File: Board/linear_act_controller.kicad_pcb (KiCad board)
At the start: 4 copper layers, 90 x 40 mm, 71 parts, among them J1 SSV, J2 ACTUATOR, J3 PROG, U1 LMR51635XDDCR, U2 MP2459, U3 MP6612, U4 STM32F030K6Tx

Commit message: WIP on routing
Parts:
- removed D6: PWR, LED_SMD:LED_0603_1608Metric_Pad1.05x0.95mm_HandSolder
- removed D7: DBG, LED_SMD:LED_0603_1608Metric
- added H1: MountingHole_Pad, MountingHole:MountingHole_3.5mm_Pad_Via, F.Cu at (59.0, 84.0)
- added H2: MountingHole_Pad, MountingHole:MountingHole_3.5mm_Pad_Via, F.Cu at (59.0, 116.0)
- added H3: MountingHole_Pad, MountingHole:MountingHole_3.5mm_Pad_Via, F.Cu at (141.0, 116.0)
- added H4: MountingHole_Pad, MountingHole:MountingHole_3.5mm_Pad_Via, F.Cu at (141.0, 84.0)
- added J4: PWR_LED, Connector_JST:JST_XH_B2B-XH-A_1x02_P2.50mm_Vertical, F.Cu at (80.0, 85.2)
- added J5: STATUS_LED, Connector_JST:JST_XH_B2B-XH-A_1x02_P2.50mm_Vertical, F.Cu at (97.0, 85.3)
- added Q9: IRLML6344TRPBF, Package_TO_SOT_SMD:SOT-23_Handsoldering, F.Cu at (88.6, 85.4)
- added R36: 10k, Resistor_SMD:R_0603_1608Metric_Pad0.98x0.95mm_HandSolder, F.Cu at (88.6, 81.6)
- R16: value 47k -> 120
- R24: value 1k -> 120
- moved D1 209.6 mm to (65.8, 91.4), turned to 180 degrees
- moved R2 205.5 mm to (66.2, 89.6), turned to 180 degrees
- moved R1 205.3 mm to (66.2, 93.2)
- moved D5 181.6 mm to (105.6, 115.0), turned to -90 degrees
- moved C9 177.4 mm to (106.8, 108.7), turned to -90 degrees
- moved C11 176.8 mm to (101.6, 115.5), turned to -90 degrees
- moved R13 176.3 mm to (101.6, 111.8), turned to 90 degrees
- moved D4 175.0 mm to (109.8, 108.4), turned to -90 degrees
- moved U2 173.3 mm to (104.2, 109.7), turned to -90 degrees
- moved C10 169.9 mm to (103.2, 115.5), turned to -90 degrees
- moved R17 167.9 mm to (100.8, 106.4), turned to 180 degrees
- moved R15 166.9 mm to (104.2, 106.4), turned to 180 degrees
- moved R16 162.9 mm to (84.0, 84.4), turned to -90 degrees
- moved C13 161.6 mm to (110.0, 115.2), turned to -90 degrees
- moved L2 160.7 mm to (108.8, 111.8)
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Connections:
- L1 pad 1: Net-(U1-SW) -> +24V
- L1 pad 2: +24V -> Net-(U1-SW)
- R24 pad 1: Net-(U4-PA13) -> +3.3V
- TP2 pad 1: Net-(U4-PA13) -> STATUS_LED
- U4 pad 23: Net-(U4-PA13) -> STATUS_LED
- U4 pad 7: HB_VISEN -> POSITION_POT
- U4 pad 8: unconnected-(U4-PA2-Pad8) -> HB_VISEN
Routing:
- net +24V: track 0.00 -> 24.2 mm, vias 0 -> 2
- net +3.3V: track 0.00 -> 11.2 mm, vias 0 -> 2
- net Net-(D4-K): track 0.00 -> 5.21 mm
- net Net-(U1-EN): track 0.00 -> 3.92 mm
- net Net-(U2-FB): track 0.00 -> 3.70 mm
- net Net-(U1-FB): track 0.00 -> 3.69 mm
- net Net-(U1-CB): track 0.00 -> 2.44 mm
- net Net-(U1-SW): track 0.00 -> 2.12 mm
- net Net-(U2-EN): track 0.00 -> 1.71 mm
- added copper zone on F.Cu, net +24V
- added copper zone on B.Cu, net Net-(D3-K)
- added copper zone on F.Cu, net Net-(D3-K)
- added copper zone on F.Cu, net Net-(D5-K)
- added copper zone on B.Cu, net Net-(U1-SW)
- added copper zone on F.Cu, net Net-(U1-SW)
- added copper zone on B.Cu, net VIN
- added copper zone on F.Cu, net VIN

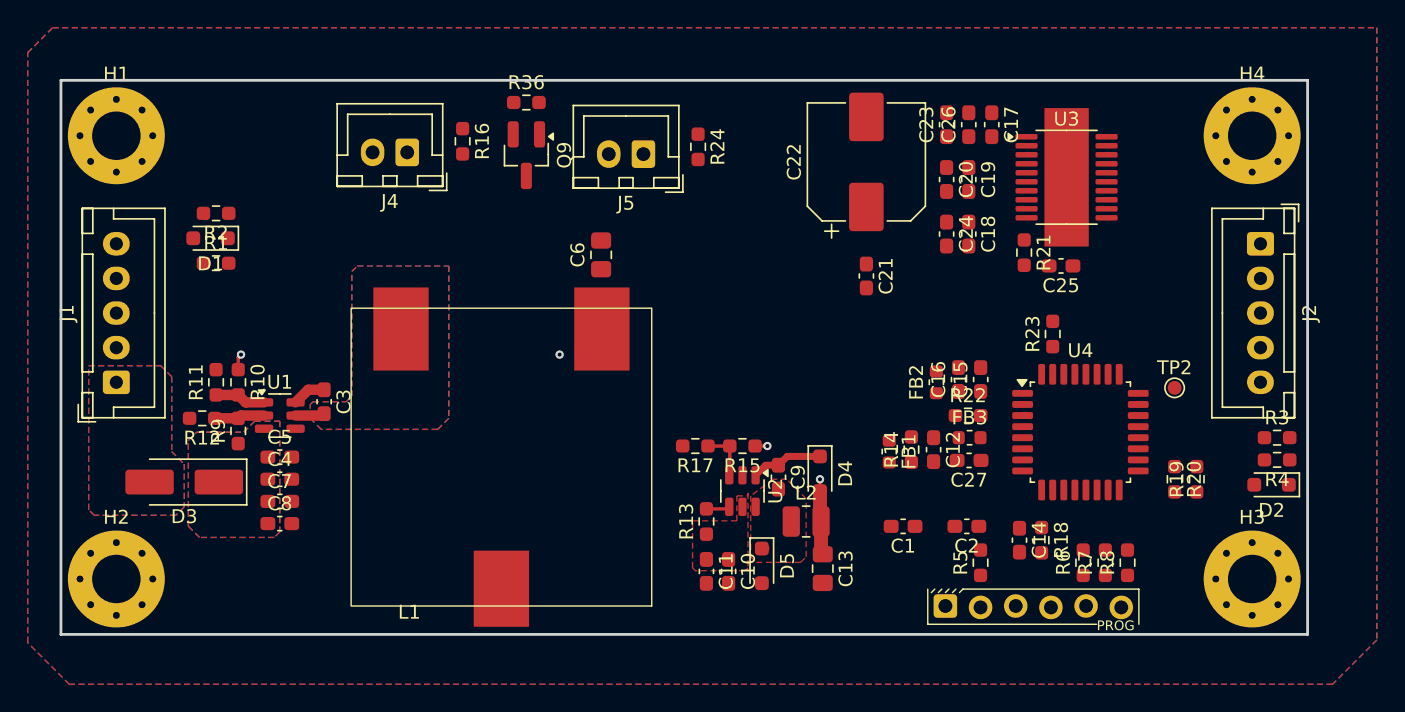
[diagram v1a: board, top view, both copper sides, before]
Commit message: Routing done, before adding polyfuse
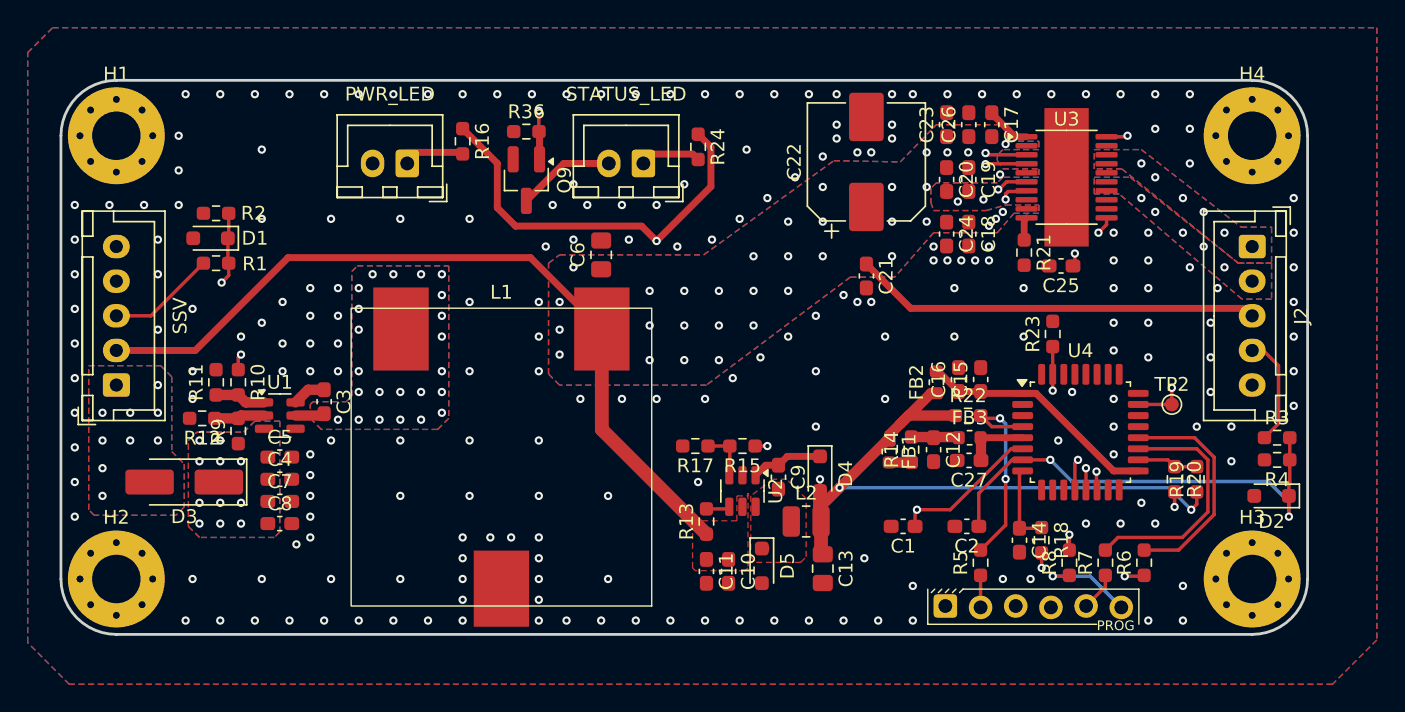
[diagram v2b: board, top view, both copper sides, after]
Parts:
- moved R6 4.40 mm to (133.2, 114.8)
- moved R8 4.20 mm to (127.8, 114.8)
- moved R36 2.10 mm to (88.6, 83.7)
- moved Q9 1.80 mm to (88.6, 87.2)
- moved TP2 1.22 mm to (135.2, 103.4)
- moved D2 0.80 mm to (142.4, 110.0)
- moved J4 0.80 mm to (80.0, 86.0)
- moved J5 0.67 mm to (97.0, 86.0)
- moved J2 0.63 mm to (141.0, 92.0)
- moved J1 0.20 mm to (59.0, 102.0)
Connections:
- L1 pad : (no net) -> GND
- U4 pad 12: HB_ENBL -> HB_DIR
- U4 pad 13: HB_DIR -> HB_ENBL
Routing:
- net +3.3V: track 11.2 -> 104.8 mm, vias 2 -> 5
- net +24V: track 24.2 -> 112.0 mm, vias 2 -> 36
- net CONTROL_POT: track 0.00 -> 75.7 mm, vias 0 -> 2
- net STATUS_LED: track 0.00 -> 70.5 mm, vias 0 -> 2
- net POSITION_POT: track 0.00 -> 33.8 mm, vias 0 -> 2
- net HB_ENBL: track 0.00 -> 31.6 mm, vias 0 -> 2
- net Net-(U3-VISEN): track 0.00 -> 31.0 mm, vias 0 -> 2
- net Net-(U3-nFAULT): track 0.00 -> 30.8 mm, vias 0 -> 2
- net HB_DIR: track 0.00 -> 30.7 mm, vias 0 -> 2
- net HB_nSLEEP: track 0.00 -> 20.0 mm, vias 0 -> 2
- net PROG_TX: track 0.00 -> 17.7 mm
- net /uC/3V3_STM: track 0.00 -> 17.6 mm
- net PROG_RX: track 0.00 -> 16.3 mm
- net PROG_NRST: track 0.00 -> 15.3 mm, vias 0 -> 2
- net PROG_BOOT0: track 0.00 -> 15.2 mm, vias 0 -> 2
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- added copper zone on B.Cu, net +24V
- added copper zone on B.Cu, net OUT1
- added copper zone on F.Cu, net OUT1
- added copper zone on B.Cu, net OUT2
- added copper zone on F.Cu, net OUT2
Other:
- outline, holes or cut-outs redrawn

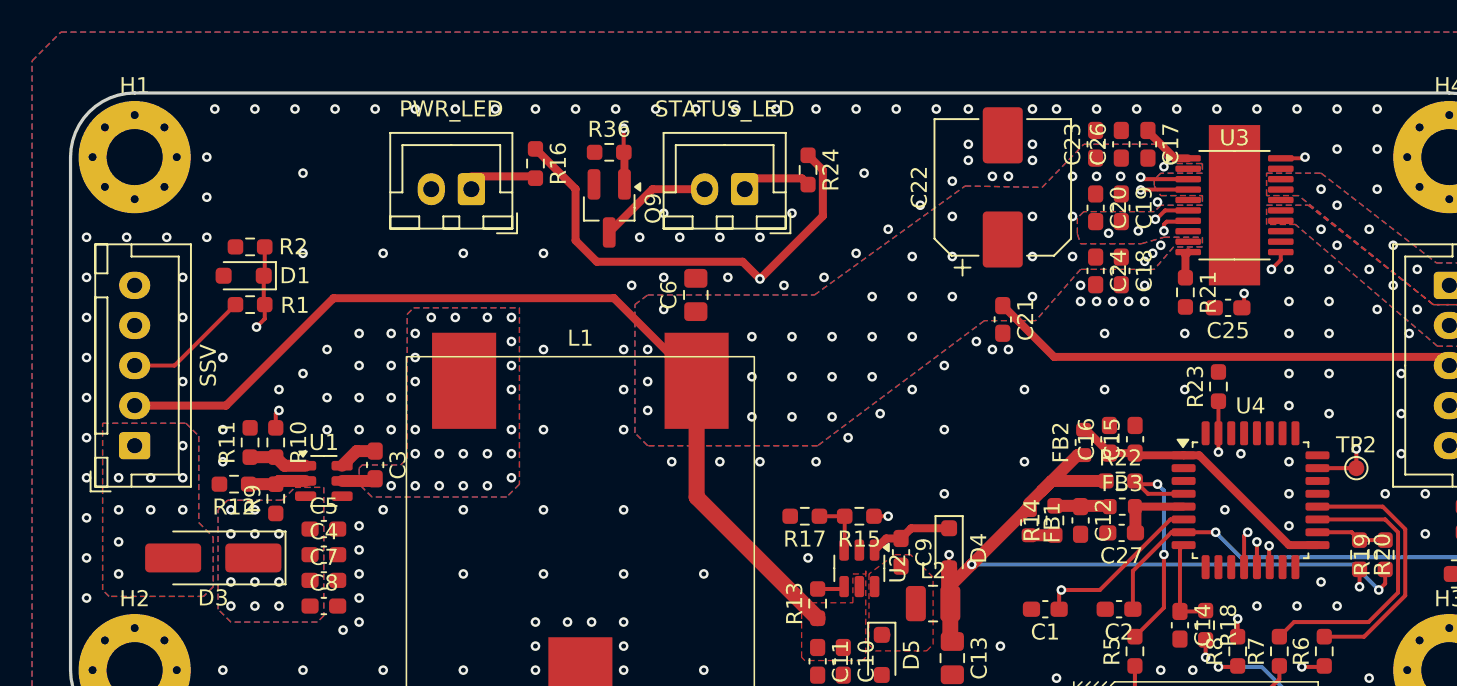
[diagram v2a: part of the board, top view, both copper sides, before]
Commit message: Routing done with polyfuse. Need to tidy silkscreen.
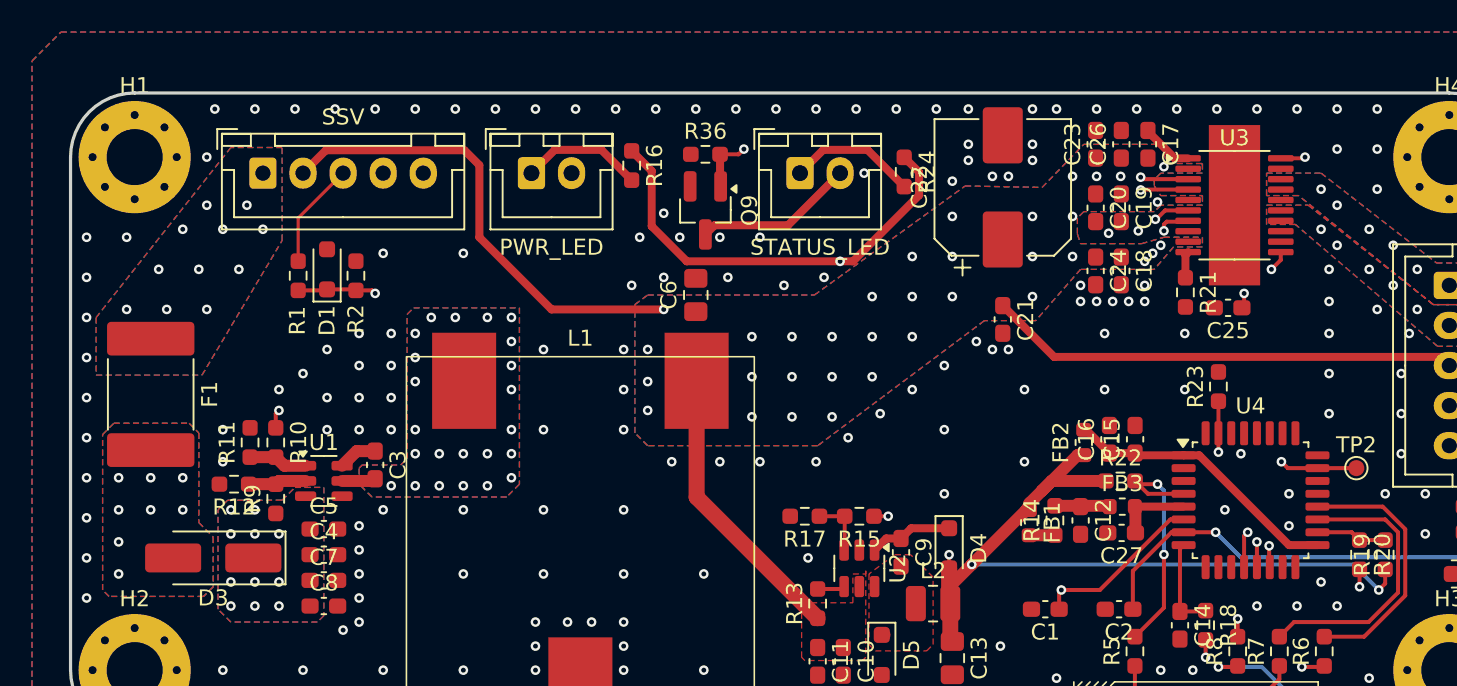
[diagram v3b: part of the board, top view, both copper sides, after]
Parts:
- added F1: SMD200F/24-2920-2, Fuse:Fuse_2920_7451Metric_Pad2.10x5.45mm_HandSolder, F.Cu at (60.0, 98.8)
- moved J1 18.8 mm to (67.0, 85.0), turned to 0 degrees
- moved R2 6.84 mm to (72.8, 91.4), turned to 90 degrees
- moved Q9 6.00 mm to (94.6, 87.3)
- moved R16 6.00 mm to (90.0, 84.5)
- moved R24 6.00 mm to (107.0, 84.9)
- moved R36 6.00 mm to (94.6, 83.8)
- moved D1 5.22 mm to (71.0, 91.0), turned to 90 degrees
- moved J4 3.88 mm to (83.8, 85.0), turned to 0 degrees
- moved J5 3.59 mm to (100.5, 85.0), turned to 0 degrees
- moved R1 3.50 mm to (69.2, 91.4), turned to -90 degrees
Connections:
- D3 pad 2: VIN -> Net-(D3-A)
- L1 pad : GND -> (no net)
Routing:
- net STATUS_LED: track 70.5 -> 58.0 mm
- net +24V: track 112.0 -> 101.9 mm
- net CONTROL_POT: track 75.7 -> 69.1 mm
- net Net-(U3-nFAULT): track 30.8 -> 36.3 mm
- net +3.3V: track 104.8 -> 100.3 mm
- net Net-(J5-Pin_1): track 4.11 -> 8.05 mm
- net Net-(J4-Pin_1): track 4.05 -> 7.63 mm
- net Net-(J5-Pin_2): track 7.07 -> 9.99 mm
- net Net-(J1-Pin_3): track 7.86 -> 6.65 mm
- net VIN: vias 9 -> 11
- net Net-(D3-A): vias 0 -> 8
- net GND: vias 219 -> 199
- added copper zone on B.Cu, net Net-(D3-A)
- added copper zone on F.Cu, net Net-(D3-A)
- added copper zone on In1.Cu, net OUT1
- added copper zone on In2.Cu, net OUT1
- added copper zone on In1.Cu, net OUT2
- added copper zone on In2.Cu, net OUT2

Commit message: Silkscreen done.
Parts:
- added U5: ~, Logos:taz, F.Cu at (105.4, 97.4)
- moved J3 2.13 mm to (98.4, 85.0)
- moved R3 2.13 mm to (104.9, 84.9)
- moved Q1 1.22 mm to (93.4, 87.1)
- moved R1 1.22 mm to (93.4, 83.6)
- moved C4 1.00 mm to (112.1, 85.9)
- renumbered C23 to C1, C25 to C10, C21 to C11, C16 to C12, C15 to C13, C3 to C14, C5 to C15, C12 to C16, C27 to C17, C4 to C18, C9 to C19, C26 to C2, C7 to C20, C8 to C21, C1 to C22, C2 to C23, C14 to C24, C11 to C25, C10 to C26, C13 to C27, C17 to C3, C22 to C4, C20 to C5, C19 to C6, C24 to C7, C18 to C8, C6 to C9, D4 to D2, D2 to D4, FB2 to FB1, FB3 to FB2, FB1 to FB3, H4 to H2, H2 to H3, H3 to H4, J4 to J2, J5 to J3, J2 to J4, J3 to J5, Q9 to Q1, R36 to R1, R12 to R10, R22 to R11, R9 to R12, R17 to R13, R15 to R14, R3 to R15, R14 to R16, R4 to R17, R20 to R18, R16 to R2, R13 to R20, R18 to R21, R5 to R22, R8 to R23, R7 to R24, R6 to R25, R24 to R3, R1 to R4, R2 to R5, R21 to R6, R23 to R7, R11 to R8, R10 to R9, TP2 to TP1, U3 to U1, U1 to U2, U4 to U3, U2 to U4
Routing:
- net STATUS_LED: track 58.0 -> 59.9 mm
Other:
- board text added: "Linear actuator controller revA https://github.com/Talw3g/linear_act_controller"

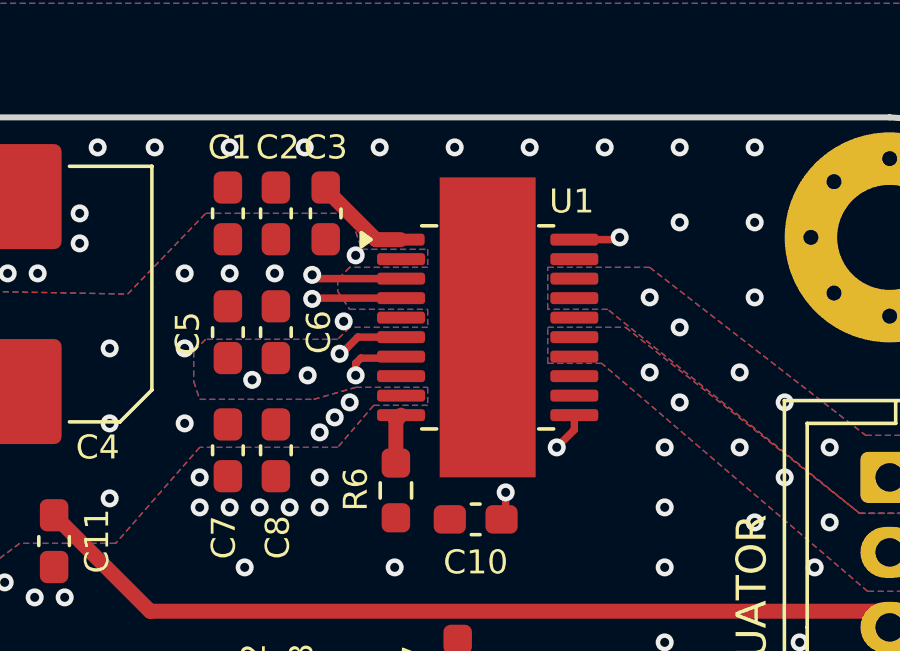
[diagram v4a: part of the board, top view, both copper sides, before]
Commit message: some 24V and GND traces to H bridge enlarged
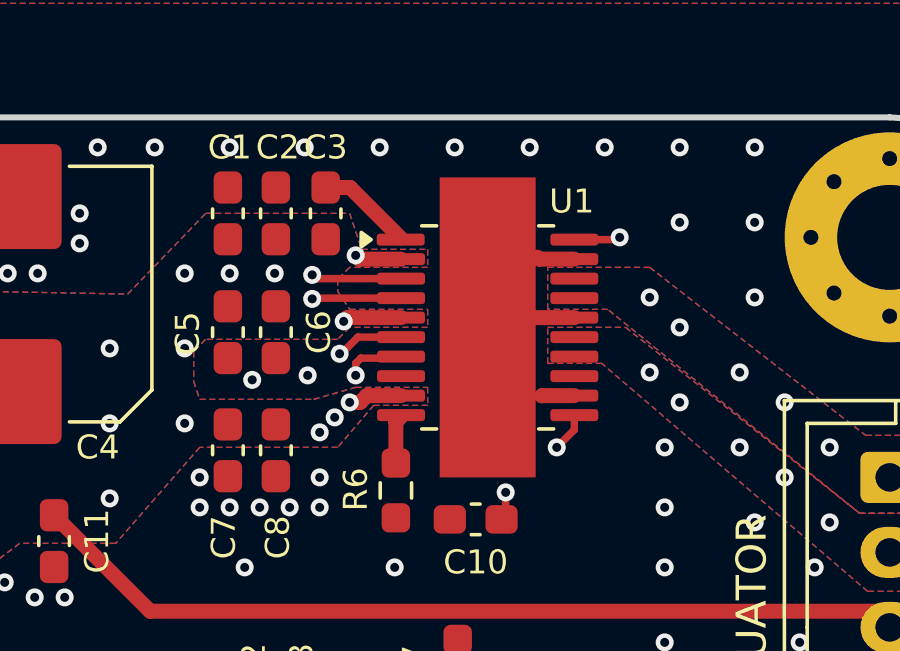
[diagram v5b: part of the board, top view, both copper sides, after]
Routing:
- net GND: track 0.00 -> 5.36 mm
- net +24V: track 101.9 -> 107.2 mm

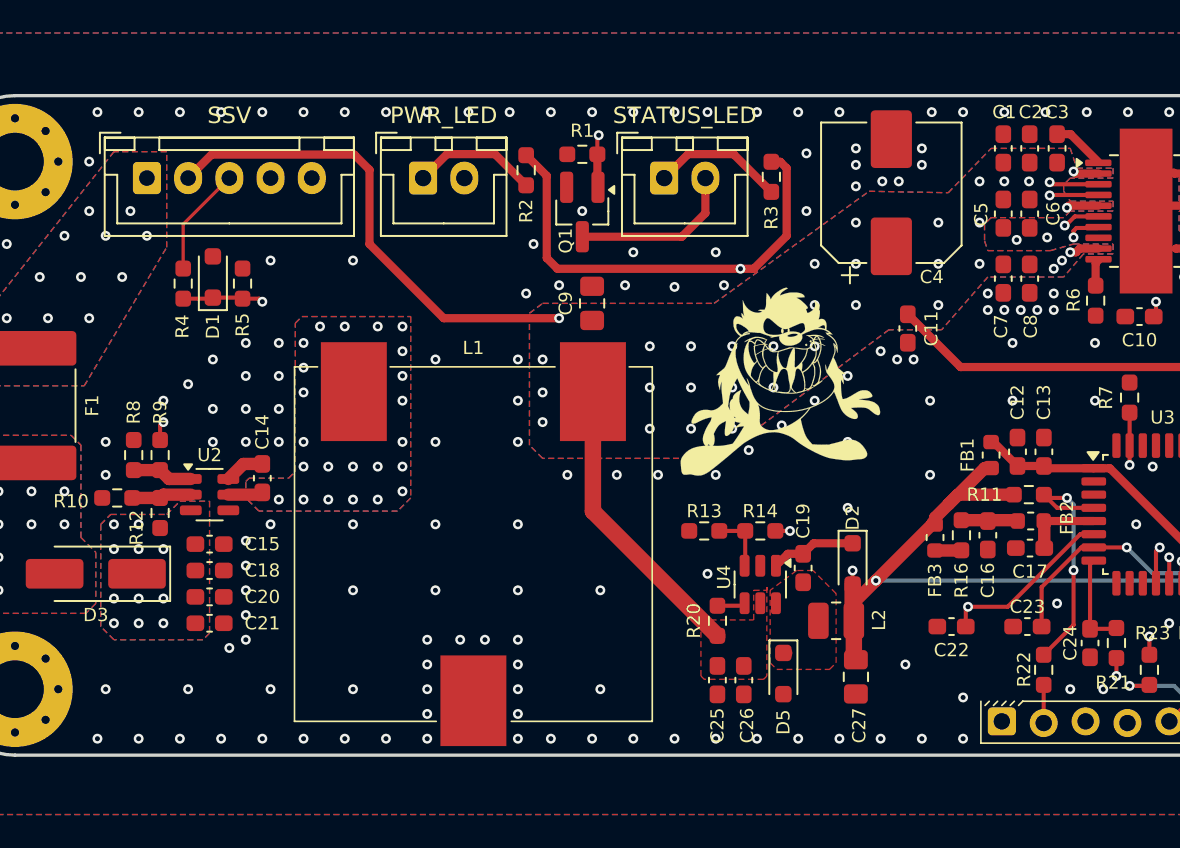
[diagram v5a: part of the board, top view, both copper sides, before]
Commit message: Changed some components based on availability.
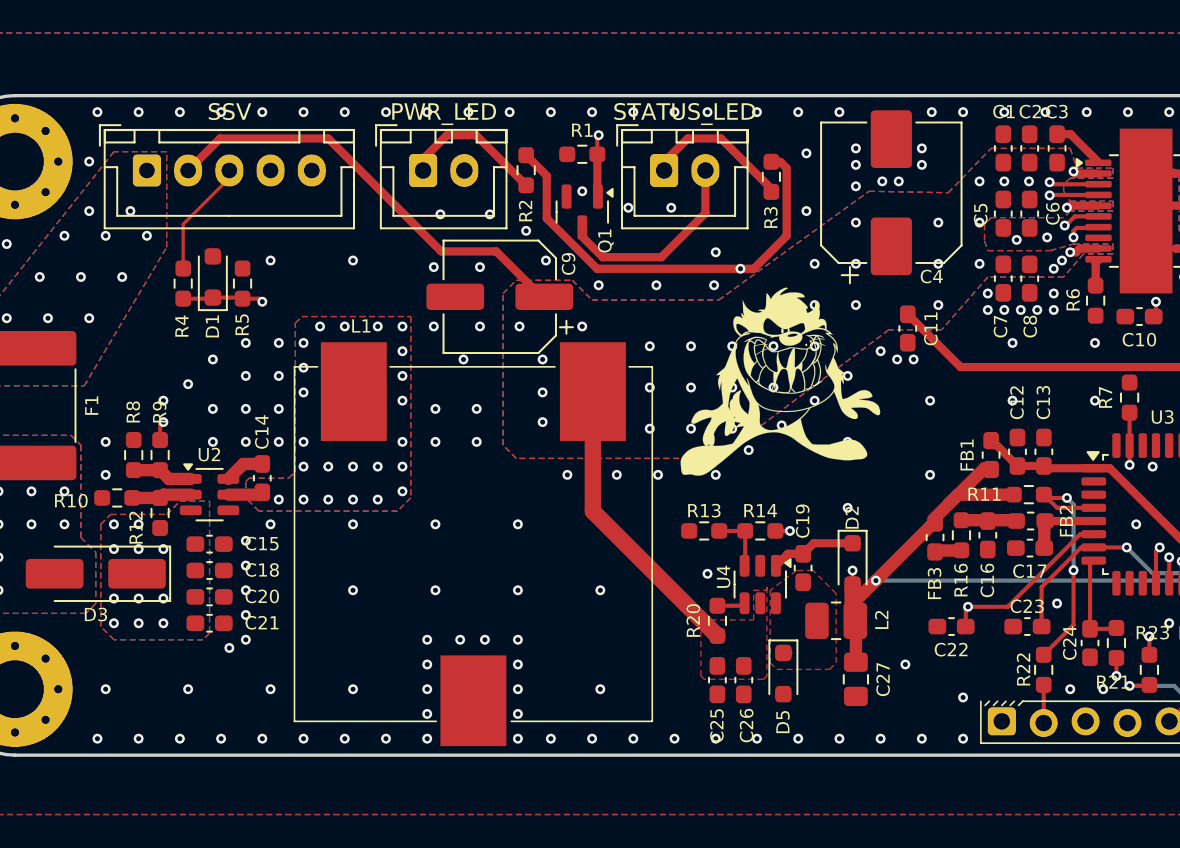
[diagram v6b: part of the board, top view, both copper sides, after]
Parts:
- C27: value 22u/35V -> 10u/16V
- C9: footprint Capacitor_SMD:C_0805_2012Metric_Pad1.18x1.45mm_HandSolder -> Capacitor_SMD:CP_Elec_6.3x5.8
- D5: value 1N5819WS -> B5819WS-TP
- FB1, FB2, FB3: footprint Inductor_SMD:L_0603_1608Metric -> Inductor_SMD:L_0603_1608Metric_Pad1.05x0.95mm_HandSolder
- L2: footprint Inductor_SMD:L_1008_2520Metric -> Inductor_SMD:L_1008_2520Metric_Pad1.43x2.20mm_HandSolder
- Q1: footprint Package_TO_SOT_SMD:SOT-23_Handsoldering -> Package_TO_SOT_SMD:SOT-23
- moved C9 5.61 mm to (88.4, 92.2), turned to 180 degrees
- moved J1 0.46 mm to (67.0, 84.5)
- moved J2 0.46 mm to (83.8, 84.5)
- moved J3 0.46 mm to (98.4, 84.5)
- moved C27 0.15 mm to (110.0, 115.4)
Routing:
- net +24V: track 107.2 -> 103.7 mm, vias 36 -> 37
- net Net-(J3-Pin_2): track 10.2 -> 11.7 mm
- net +3.3V: track 100.7 -> 99.5 mm
- net Net-(J2-Pin_1): track 7.63 -> 8.80 mm
- net Net-(J3-Pin_1): track 8.05 -> 9.05 mm
- net GND: vias 199 -> 205
